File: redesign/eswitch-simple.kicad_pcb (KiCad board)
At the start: 4 copper layers, 176 x 116 mm, 210 parts, among them J11 CH1 OUTPUT, J12 CH2 OUTPUT, J13 CH3 OUTPUT, J14 CH4 OUTPUT, J15 CH5 OUTPUT, J16 CH6 OUTPUT, J17 CH7 OUTPUT, J18 CH8 OUTPUT, J2 BATT_RAW, J3 GND, J4 USB-C, J5 UART, Q5 BSC016N06NS, SW1 RESET, SW2 BOOT, U1 BTS7004-1EPP, U10 ESP32-S3-WROOM-1-N8, U11 SRV05-4HTG-D, U13 LM74800-Q1, U14 TLA431AIDBZR, U2 BTS7004-1EPP, U3 BTS7008-1EPR, U4 BTS7008-1EPR, U5 BTS7008-1EPR, U6 BTS7008-1EPR, U7 BTS7008-1EPR, U8 BTS7002-1EPP, U9 TPSM63603V3

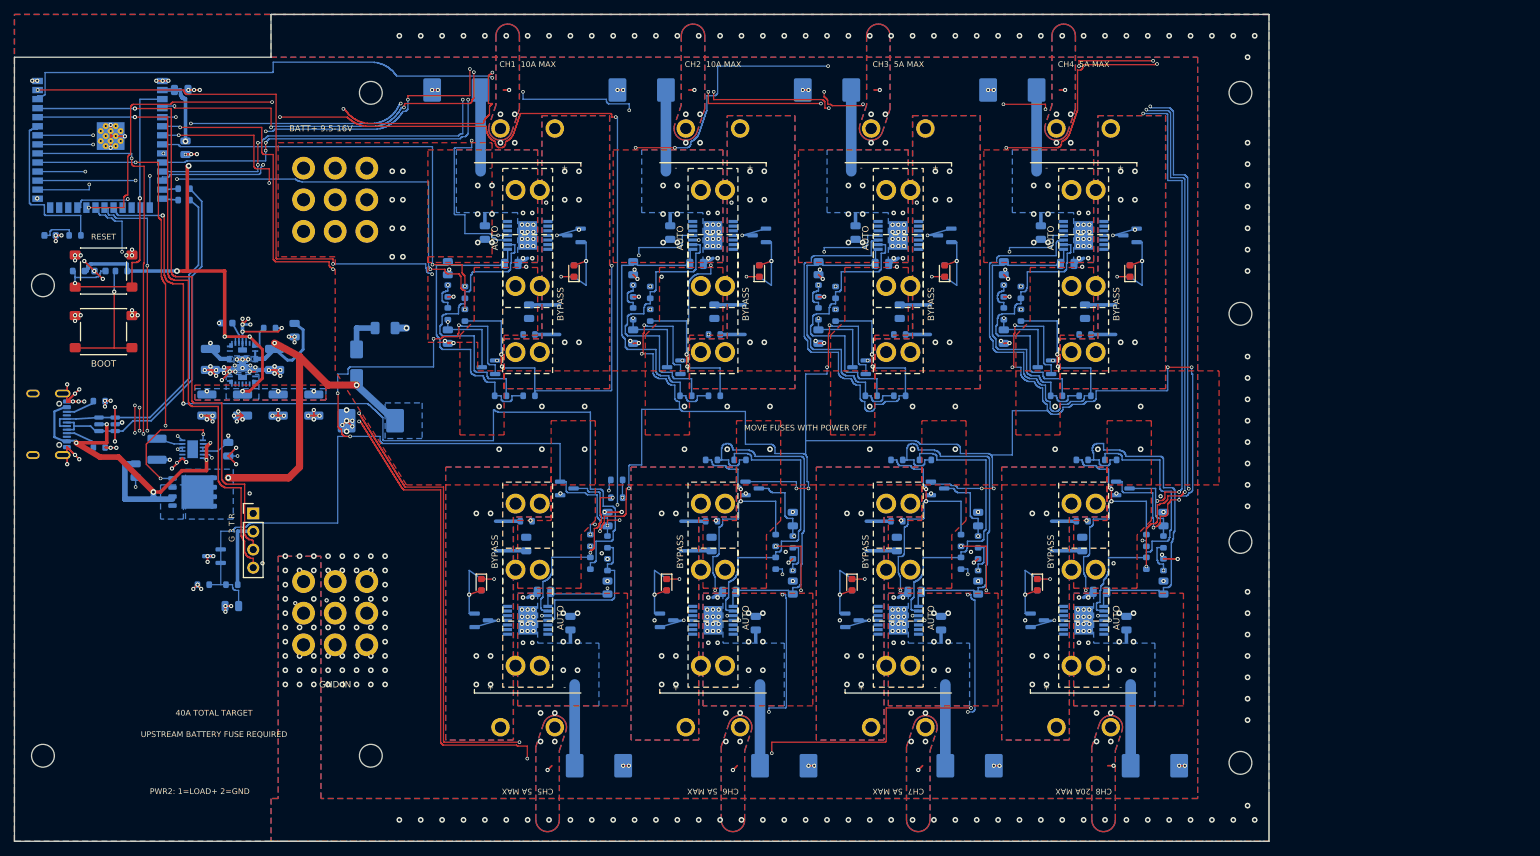
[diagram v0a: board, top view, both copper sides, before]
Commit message: Release PROTO-PWR3 shared AUTO protection and passive bypass prototype
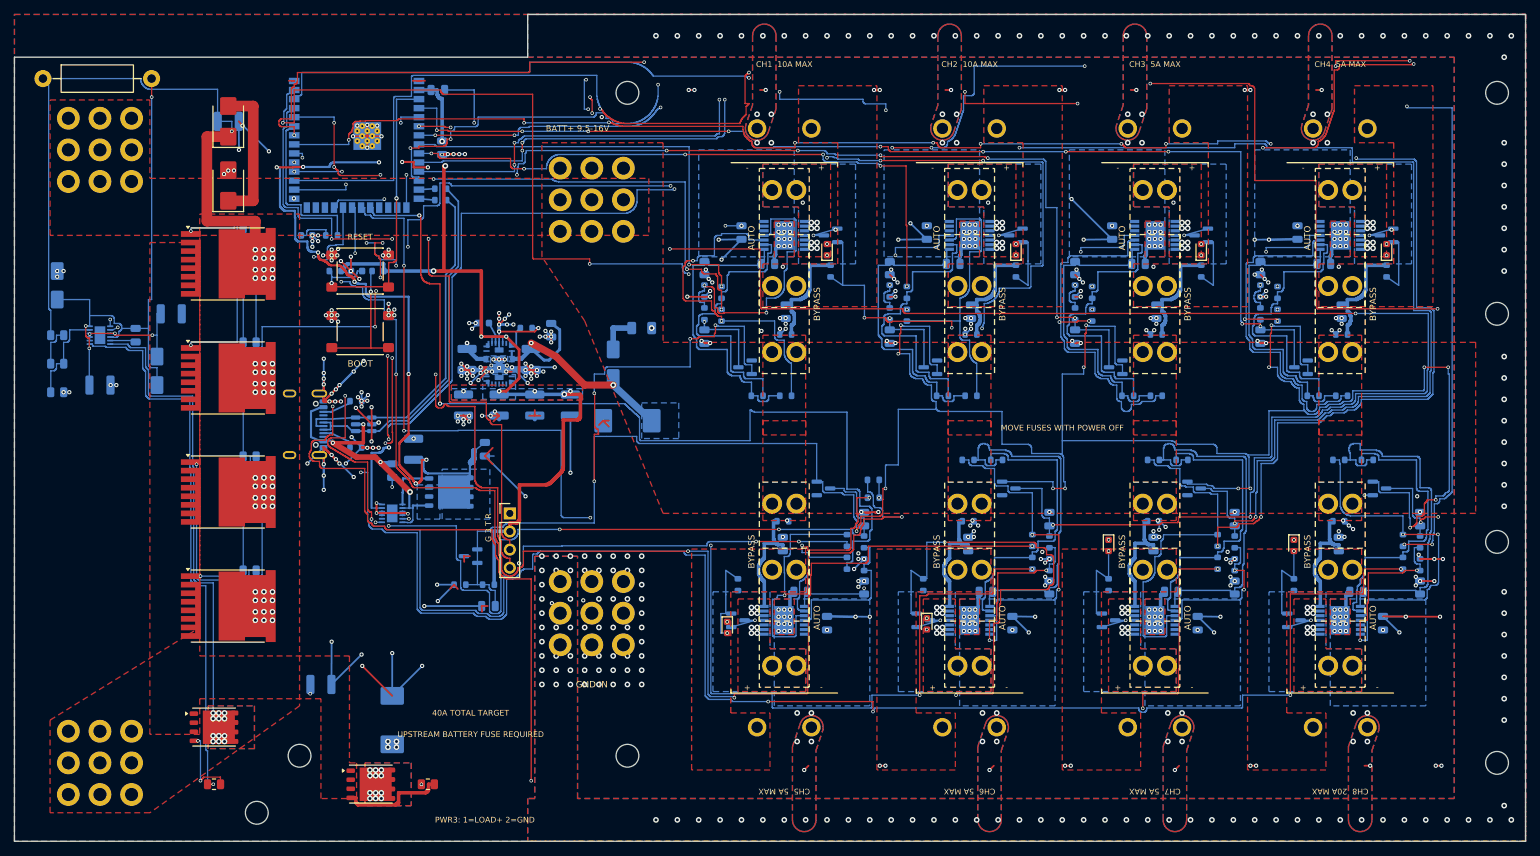
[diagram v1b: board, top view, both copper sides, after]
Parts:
- removed D104, D204, D304, D404, D504, D604, D704, D804: SMCJ16A, Diode_SMD:D_SMC
- added C25: 100nF 250V, Capacitor_SMD:C_1210_3225Metric, B.Cu at (30.0, 15.0)
- added C26: 1uF 100V, Capacitor_SMD:C_1210_3225Metric, B.Cu at (12.0, 52.0)
- added C27: 1uF 50V, Capacitor_SMD:C_0805_2012Metric, B.Cu at (17.0, 45.0)
- added C28: 1uF 100V, Capacitor_SMD:C_1210_3225Metric, B.Cu at (22.0, 42.0)
- added C29: 4.7uF 50V, Capacitor_SMD:C_1210_3225Metric, B.Cu at (43.0, 94.0)
- added D10: SMCJ16A LOCAL TRANSIENT, Diode_SMD:D_SMC, B.Cu at (53.0, 99.0)
- added D6: SMBJ150A, Diode_SMD:D_SMB, F.Cu at (30.0, 15.0)
- added D7: SMBJ33CA, Diode_SMD:D_SMB, F.Cu at (30.0, 24.0)
- added D8: 51V 2%, Diode_SMD:D_SMA, B.Cu at (6.00, 38.0)
- added D9: 82V, Diode_SMD:D_SMA, B.Cu at (20.0, 50.0)
- added F10: 40A AUTO/LOGIC ISOLATION, eswitch:Fuse_Mersen_14x51_MR14_Wuerth_M5, F.Cu at (12.0, 62.0)
- added Q10: BSC016N06NS 60V, Package_SON:Infineon_PG-TDSON-8_6.15x5.15mm, F.Cu at (28.0, 100.0)
- added Q11: BSC016N06NS 60V, Package_SON:Infineon_PG-TDSON-8_6.15x5.15mm, F.Cu at (50.0, 108.0)
- added Q6: IPT067N20NM6 200V, Package_TO_SOT_SMD:Infineon_PG-HSOF-8-1, F.Cu at (30.0, 35.0)
- added Q7: IPT067N20NM6 200V, Package_TO_SOT_SMD:Infineon_PG-HSOF-8-1, F.Cu at (30.0, 51.0)
- added Q8: IPT067N20NM6 200V, Package_TO_SOT_SMD:Infineon_PG-HSOF-8-1, F.Cu at (30.0, 67.0)
- added Q9: IPT067N20NM6 200V, Package_TO_SOT_SMD:Infineon_PG-HSOF-8-1, F.Cu at (30.0, 83.0)
- added R20: 10R, Resistor_SMD:R_0805_2012Metric, B.Cu at (33.0, 30.0)
- added R21: 10R, Resistor_SMD:R_0805_2012Metric, B.Cu at (33.0, 46.0)
- added R22: 10R, Resistor_SMD:R_0805_2012Metric, B.Cu at (33.0, 62.0)
- added R23: 10R, Resistor_SMD:R_0805_2012Metric, B.Cu at (33.0, 78.0)
- added R24: 10R, Resistor_SMD:R_0805_2012Metric, F.Cu at (28.0, 108.0)
- added R25: 10R, Resistor_SMD:R_0805_2012Metric, F.Cu at (58.0, 108.0)
- added R26: 4.7k 2W, Resistor_THT:R_Axial_DIN0411_L9.9mm_D3.6mm_P15.24mm_Horizontal, F.Cu at (4.00, 9.00)
- added R27: 49.9k 0.1%, Resistor_SMD:R_0805_2012Metric, B.Cu at (6.00, 45.0)
- added R28: 49.9k 0.1%, Resistor_SMD:R_0805_2012Metric, B.Cu at (6.00, 49.0)
- added R29: 7.87k 0.1%, Resistor_SMD:R_0805_2012Metric, B.Cu at (6.00, 53.0)
- added U15: LM74800-Q1 AUTO CUTOFF, Package_SON:WSON-12-1EP_3x3mm_P0.5mm_EP1.5x2.5mm, B.Cu at (12.0, 45.0)
- moved H1 79.8 mm to (34.0, 112.0)
- moved D602 36.9 mm to (128.0, 85.5)
- moved D702 36.4 mm to (153.5, 74.5)
- moved D802 36.4 mm to (179.5, 74.5)
- moved D202 36.1 mm to (140.5, 33.0)
- moved D302 36.1 mm to (166.5, 33.0)
- moved D402 36.1 mm to (192.5, 33.0)
- moved C303 36.0 mm to (148.8, 45.2)
- moved C602 36.0 mm to (133.8, 74.3)
- moved C604 36.0 mm to (136.3, 81.0)
- moved C702 36.0 mm to (159.8, 74.3)
- moved C704 36.0 mm to (162.3, 81.0)
- moved R303 36.0 mm to (148.8, 35.6)
- moved R304 36.0 mm to (148.8, 38.8)
- moved R305 36.0 mm to (148.8, 42.0)
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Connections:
- C101 pad 1: /VS1 -> /AUTO_PROTECTED
- C102 pad 1: /LOAD1 -> /PROFET_OUT1
- C104 pad 1: /VS1 -> /AUTO_PROTECTED
- C201 pad 1: /VS2 -> /AUTO_PROTECTED
- C202 pad 1: /LOAD2 -> /PROFET_OUT2
- C204 pad 1: /VS2 -> /AUTO_PROTECTED
- C301 pad 1: /VS3 -> /AUTO_PROTECTED
- C302 pad 1: /LOAD3 -> /PROFET_OUT3
- C304 pad 1: /VS3 -> /AUTO_PROTECTED
- C401 pad 1: /VS4 -> /AUTO_PROTECTED
- C402 pad 1: /LOAD4 -> /PROFET_OUT4
- C404 pad 1: /VS4 -> /AUTO_PROTECTED
- C501 pad 1: /VS5 -> /AUTO_PROTECTED
- C502 pad 1: /LOAD5 -> /PROFET_OUT5
- C504 pad 1: /VS5 -> /AUTO_PROTECTED
- C601 pad 1: /VS6 -> /AUTO_PROTECTED
- C602 pad 1: /LOAD6 -> /PROFET_OUT6
- C604 pad 1: /VS6 -> /AUTO_PROTECTED
- C701 pad 1: /VS7 -> /AUTO_PROTECTED
- C702 pad 1: /LOAD7 -> /PROFET_OUT7
- C704 pad 1: /VS7 -> /AUTO_PROTECTED
- C801 pad 1: /VS8 -> /AUTO_PROTECTED
- C802 pad 1: /LOAD8 -> /PROFET_OUT8
- C804 pad 1: /VS8 -> /AUTO_PROTECTED
- F1 pad 1: /VS1 -> /PROFET_OUT1
- F1 pad 2: /BATT_RAW -> /LOAD1
- F1 pad 3: /LOAD1 -> /BATT_RAW
- F2 pad 1: /VS2 -> /PROFET_OUT2
- F2 pad 2: /BATT_RAW -> /LOAD2
- F2 pad 3: /LOAD2 -> /BATT_RAW
- F3 pad 1: /VS3 -> /PROFET_OUT3
- F3 pad 2: /BATT_RAW -> /LOAD3
- F3 pad 3: /LOAD3 -> /BATT_RAW
- F4 pad 1: /VS4 -> /PROFET_OUT4
- F4 pad 2: /BATT_RAW -> /LOAD4
- F4 pad 3: /LOAD4 -> /BATT_RAW
- F5 pad 1: /VS5 -> /PROFET_OUT5
- F5 pad 2: /BATT_RAW -> /LOAD5
- F5 pad 3: /LOAD5 -> /BATT_RAW
- F6 pad 1: /VS6 -> /PROFET_OUT6
- F6 pad 2: /BATT_RAW -> /LOAD6
- F6 pad 3: /LOAD6 -> /BATT_RAW
- F7 pad 1: /VS7 -> /PROFET_OUT7
- F7 pad 2: /BATT_RAW -> /LOAD7
- F7 pad 3: /LOAD7 -> /BATT_RAW
- F8 pad 1: /VS8 -> /PROFET_OUT8
- F8 pad 2: /BATT_RAW -> /LOAD8
- F8 pad 3: /LOAD8 -> /BATT_RAW
- F9 pad 1: /BATT_RAW -> /AUTO_PROTECTED
- R106 pad 1: /LOAD1 -> /PROFET_OUT1
- R107 pad 1: /LOAD1 -> /PROFET_OUT1
- R206 pad 1: /LOAD2 -> /PROFET_OUT2
- R207 pad 1: /LOAD2 -> /PROFET_OUT2
- R306 pad 1: /LOAD3 -> /PROFET_OUT3
- R307 pad 1: /LOAD3 -> /PROFET_OUT3
- R406 pad 1: /LOAD4 -> /PROFET_OUT4
- R407 pad 1: /LOAD4 -> /PROFET_OUT4
- R506 pad 1: /LOAD5 -> /PROFET_OUT5
- R507 pad 1: /LOAD5 -> /PROFET_OUT5
- R606 pad 1: /LOAD6 -> /PROFET_OUT6
- R607 pad 1: /LOAD6 -> /PROFET_OUT6
- R706 pad 1: /LOAD7 -> /PROFET_OUT7
- R707 pad 1: /LOAD7 -> /PROFET_OUT7
- R806 pad 1: /LOAD8 -> /PROFET_OUT8
- R807 pad 1: /LOAD8 -> /PROFET_OUT8
- U1 pad 10: /LOAD1 -> /PROFET_OUT1
- U1 pad 12: /LOAD1 -> /PROFET_OUT1
- U1 pad 13: /LOAD1 -> /PROFET_OUT1
- U1 pad 14: /LOAD1 -> /PROFET_OUT1
- U1 pad 15: /VS1 -> /AUTO_PROTECTED
- U1 pad 8: /LOAD1 -> /PROFET_OUT1
- U1 pad 9: /LOAD1 -> /PROFET_OUT1
- U2 pad 10: /LOAD2 -> /PROFET_OUT2
- U2 pad 12: /LOAD2 -> /PROFET_OUT2
- U2 pad 13: /LOAD2 -> /PROFET_OUT2
- U2 pad 14: /LOAD2 -> /PROFET_OUT2
- U2 pad 15: /VS2 -> /AUTO_PROTECTED
- U2 pad 8: /LOAD2 -> /PROFET_OUT2
- U2 pad 9: /LOAD2 -> /PROFET_OUT2
- U3 pad 10: /LOAD3 -> /PROFET_OUT3
- U3 pad 12: /LOAD3 -> /PROFET_OUT3
- U3 pad 13: /LOAD3 -> /PROFET_OUT3
- U3 pad 14: /LOAD3 -> /PROFET_OUT3
- U3 pad 15: /VS3 -> /AUTO_PROTECTED
- U3 pad 8: /LOAD3 -> /PROFET_OUT3
- U3 pad 9: /LOAD3 -> /PROFET_OUT3
- U4 pad 10: /LOAD4 -> /PROFET_OUT4
- U4 pad 12: /LOAD4 -> /PROFET_OUT4
- U4 pad 13: /LOAD4 -> /PROFET_OUT4
- U4 pad 14: /LOAD4 -> /PROFET_OUT4
- U4 pad 15: /VS4 -> /AUTO_PROTECTED
- U4 pad 8: /LOAD4 -> /PROFET_OUT4
- U4 pad 9: /LOAD4 -> /PROFET_OUT4
- U5 pad 10: /LOAD5 -> /PROFET_OUT5
- U5 pad 12: /LOAD5 -> /PROFET_OUT5
- U5 pad 13: /LOAD5 -> /PROFET_OUT5
- U5 pad 14: /LOAD5 -> /PROFET_OUT5
- U5 pad 15: /VS5 -> /AUTO_PROTECTED
- U5 pad 8: /LOAD5 -> /PROFET_OUT5
- U5 pad 9: /LOAD5 -> /PROFET_OUT5
- U6 pad 10: /LOAD6 -> /PROFET_OUT6
- U6 pad 12: /LOAD6 -> /PROFET_OUT6
- U6 pad 13: /LOAD6 -> /PROFET_OUT6
- U6 pad 14: /LOAD6 -> /PROFET_OUT6
- U6 pad 15: /VS6 -> /AUTO_PROTECTED
- U6 pad 8: /LOAD6 -> /PROFET_OUT6
- U6 pad 9: /LOAD6 -> /PROFET_OUT6
- U7 pad 10: /LOAD7 -> /PROFET_OUT7
- U7 pad 12: /LOAD7 -> /PROFET_OUT7
- U7 pad 13: /LOAD7 -> /PROFET_OUT7
- U7 pad 14: /LOAD7 -> /PROFET_OUT7
- U7 pad 15: /VS7 -> /AUTO_PROTECTED
- U7 pad 8: /LOAD7 -> /PROFET_OUT7
- U7 pad 9: /LOAD7 -> /PROFET_OUT7
- U8 pad 10: /LOAD8 -> /PROFET_OUT8
- U8 pad 12: /LOAD8 -> /PROFET_OUT8
- U8 pad 13: /LOAD8 -> /PROFET_OUT8
- U8 pad 14: /LOAD8 -> /PROFET_OUT8
- U8 pad 15: /VS8 -> /AUTO_PROTECTED
- U8 pad 8: /LOAD8 -> /PROFET_OUT8
- U8 pad 9: /LOAD8 -> /PROFET_OUT8
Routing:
- net /AUTO_PROTECTED: track 0.00 -> 600.7 mm, vias 0 -> 135
- net /GND: track 196.2 -> 525.9 mm, vias 440 -> 536
- net /HGATE_AUTO: track 0.00 -> 156.0 mm, vias 0 -> 3
- net /DGATE_AUTO: track 0.00 -> 115.7 mm, vias 0 -> 2
- net /DEN4: track 232.7 -> 342.4 mm, vias 4 -> 10
- net /LEDK1: track 10.7 -> 112.7 mm, vias 1 -> 7
- net /AUTO_FUSED: track 0.00 -> 99.4 mm, vias 0 -> 49
- net /VIN: track 111.5 -> 207.7 mm, vias 8 -> 16
- net /BATT_RAW: track 1.60 -> 92.6 mm, vias 33 -> 0
- net /VS_CONTROLLER: track 0.00 -> 75.5 mm, vias 0 -> 3
- net /LEDK6: track 10.7 -> 80.8 mm, vias 1 -> 3
- net /DENR1: track 118.8 -> 50.3 mm, vias 4 -> 2
- net /DEN2: track 285.4 -> 347.4 mm, vias 7 -> 13
- net /HGATE_Q8: track 0.00 -> 46.5 mm, vias 0 -> 1
- net /IS6: track 217.7 -> 262.2 mm, vias 5 -> 6
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- added copper zone on F.Cu, net /AUTO_FUSED
- added copper zone on In2.Cu, net /AUTO_FUSED
- added copper zone on B.Cu, net /AUTO_PROTECTED
- added copper zone on F.Cu, net /AUTO_PROTECTED
- added copper zone on In2.Cu, net /AUTO_PROTECTED
- added copper zone on B.Cu, net /PROFET_OUT1
- added copper zone on F.Cu, net /PROFET_OUT1
- added copper zone on B.Cu, net /PROFET_OUT2
- added copper zone on F.Cu, net /PROFET_OUT2
- added copper zone on B.Cu, net /PROFET_OUT3
- added copper zone on F.Cu, net /PROFET_OUT3
- added copper zone on B.Cu, net /PROFET_OUT4
- added copper zone on F.Cu, net /PROFET_OUT4
- added copper zone on B.Cu, net /PROFET_OUT5
- added copper zone on F.Cu, net /PROFET_OUT5
- added copper zone on B.Cu, net /PROFET_OUT6
- added copper zone on F.Cu, net /PROFET_OUT6
- added copper zone on B.Cu, net /PROFET_OUT7
- added copper zone on F.Cu, net /PROFET_OUT7
- added copper zone on B.Cu, net /PROFET_OUT8
- added copper zone on F.Cu, net /PROFET_OUT8
- added copper zone on F.Cu, net /PROTECTION_COMMON_SOURCE
- removed copper zone on In2.Cu, net /BATT_RAW
- removed copper zone on B.Cu, net /LOAD1
- removed copper zone on B.Cu, net /LOAD2
- removed copper zone on B.Cu, net /LOAD3
- removed copper zone on B.Cu, net /LOAD4
- removed copper zone on B.Cu, net /LOAD5
- removed copper zone on B.Cu, net /LOAD6
- removed copper zone on B.Cu, net /LOAD7
- removed copper zone on B.Cu, net /LOAD8
- removed copper zone on B.Cu, net /VS1
- removed copper zone on F.Cu, net /VS1
- removed copper zone on In2.Cu, net /VS1
- removed copper zone on B.Cu, net /VS2
- removed copper zone on F.Cu, net /VS2
- removed copper zone on In2.Cu, net /VS2
- removed copper zone on B.Cu, net /VS3
- removed copper zone on F.Cu, net /VS3
- removed copper zone on In2.Cu, net /VS3
- removed copper zone on B.Cu, net /VS4
- removed copper zone on F.Cu, net /VS4
- removed copper zone on In2.Cu, net /VS4
- removed copper zone on B.Cu, net /VS5
- removed copper zone on F.Cu, net /VS5
- removed copper zone on In2.Cu, net /VS5
- removed copper zone on B.Cu, net /VS6
- removed copper zone on F.Cu, net /VS6
- removed copper zone on In2.Cu, net /VS6
- removed copper zone on B.Cu, net /VS7
- removed copper zone on F.Cu, net /VS7
- removed copper zone on In2.Cu, net /VS7
- removed copper zone on B.Cu, net /VS8
- removed copper zone on F.Cu, net /VS8
- removed copper zone on In2.Cu, net /VS8
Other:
- board size 176 x 116 mm -> 212 x 116 mm
- board text added: "PWR3: 1=LOAD+ 2=GND"
- board text removed: "PWR2: 1=LOAD+ 2=GND"
